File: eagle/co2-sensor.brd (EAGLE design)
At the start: 34 x 30 mm, 12 parts, among them IC1 LM1117IMPX-3.3, J1 MH-Z19, U1 esp12e, U2 dht22, X1 usb

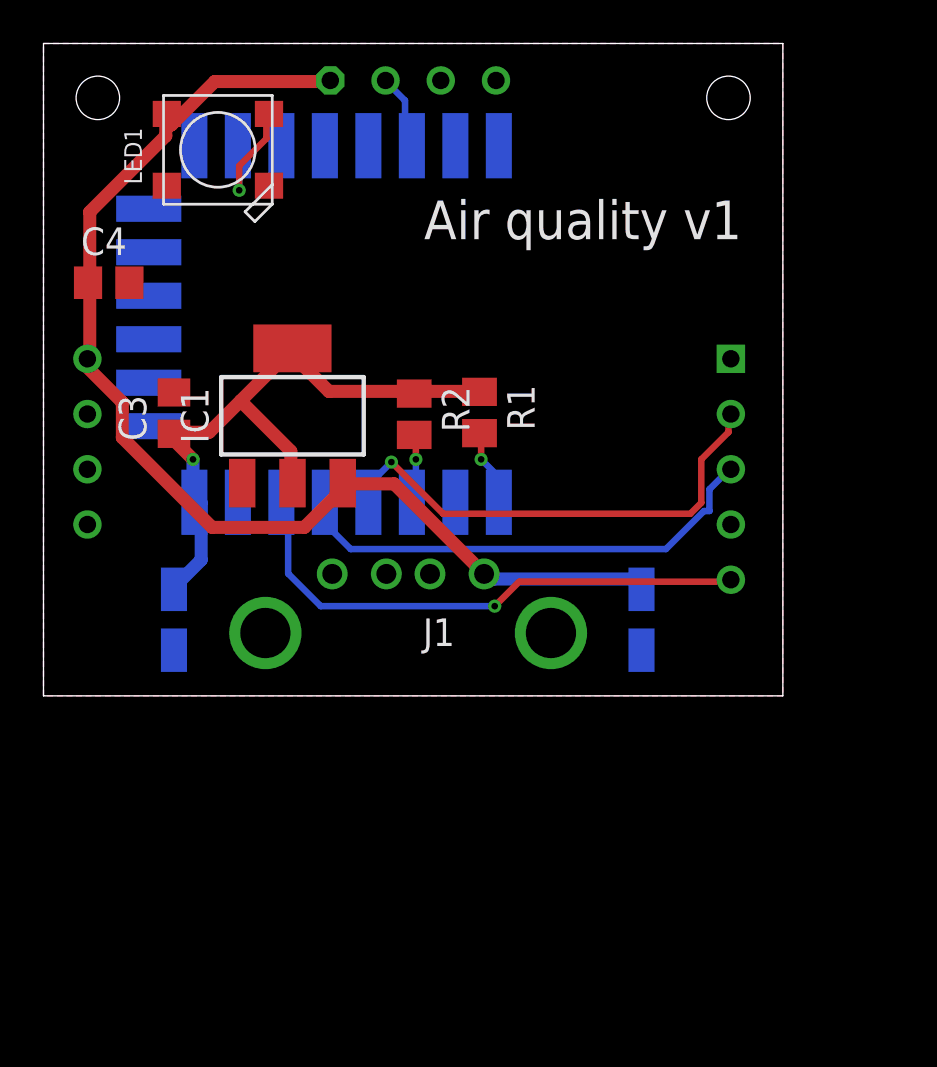
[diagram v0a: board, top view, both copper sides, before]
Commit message: fixed prototype issues
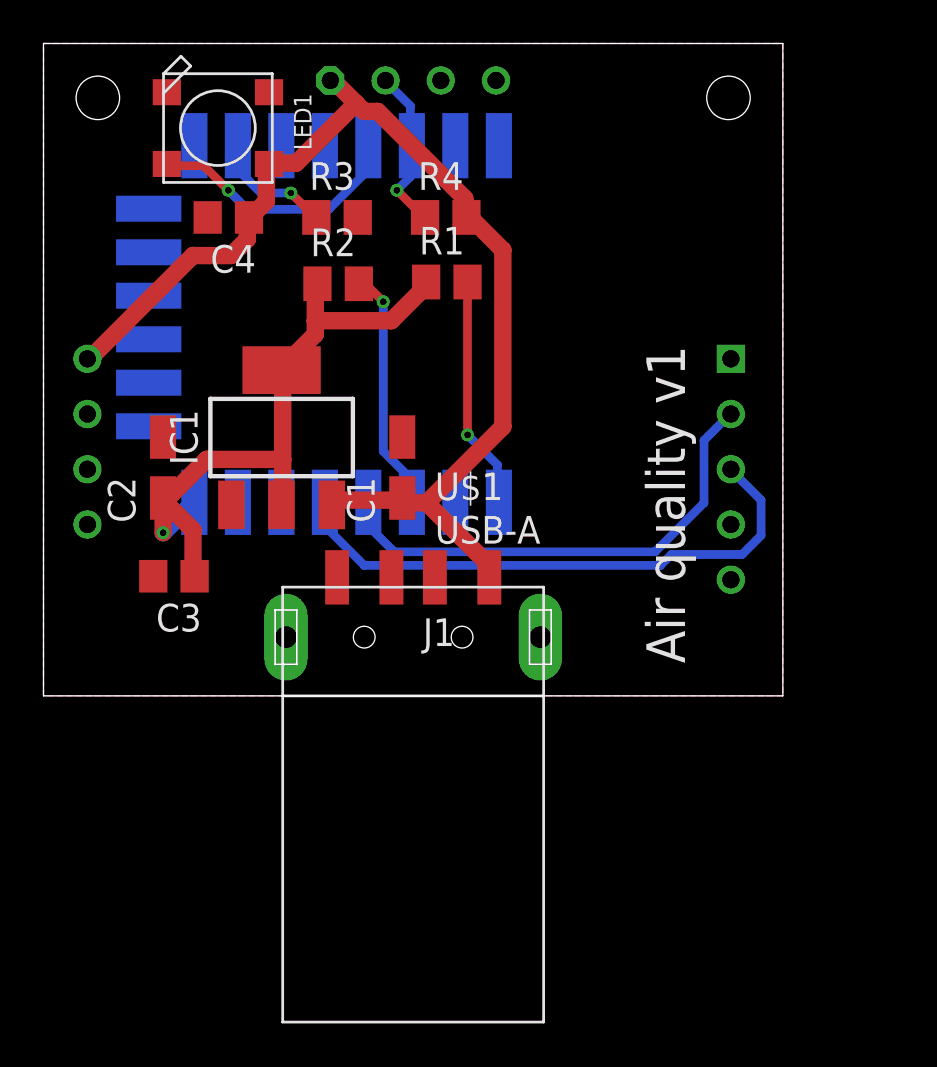
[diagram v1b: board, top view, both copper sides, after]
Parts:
- removed X1: usb, con-usb-3:USB-A-H
- added R3: 4.7k, rcl:M0805
- added R4: 10k, rcl:M0805
- added U$1: USB-A, usb:USB-A-SMT
- moved C1 13.0 mm to (16.5, 10.5), flipped to the top, turned to 90 degrees
- moved C3 7.50 mm to (6.00, 5.50), turned to 180 degrees
- moved C2 7.02 mm to (5.50, 10.5), flipped to the top, turned to 90 degrees
- moved R2 6.95 mm to (13.6, 18.9), turned to 0 degrees
- moved C4 6.26 mm to (8.50, 22.0), turned to 180 degrees
- moved R1 6.18 mm to (18.6, 19.0), turned to 0 degrees
- moved IC1 1.12 mm to (10.9, 11.9)
- moved LED1 1.00 mm to (8.02, 26.1), turned to 0 degrees
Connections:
- net CO2_VO renamed VO
- removed net CO2_HD: J1.5, U1.GPIO12
- removed net LED_DIN: LED1.4-DIN, U1.GPIO15
- new net LED: LED1.4-DIN, U1.GPIO4
- new net N$1: R3.1, U1.GPIO15
- net +5V: now also R4.2, U$1.P$6; no longer X1.VBUS
- net DHT22: now also R4.1
- net GND: now also R3.2, U$1.P$3; no longer X1.GND
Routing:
- net CO2_HD: track 25.0 -> 0.00 mm, vias 1 -> 0
- net LED: track 0.00 -> 12.0 mm, vias 0 -> 1
- net CH_PD: track 3.32 -> 11.3 mm
- net RESET: track 3.54 -> 10.7 mm
- net LED_DIN: track 6.22 -> 0.00 mm, vias 1 -> 0
- net N$1: track 0.00 -> 5.63 mm, vias 0 -> 1
- net DHT22: track 3.64 -> 7.64 mm, vias 0 -> 1
- net CO2_TX: track 22.2 -> 26.1 mm
- net +5V: track 54.7 -> 52.8 mm
- net +3V3: track 30.0 -> 31.0 mm
- net CO2_RX: track 22.4 -> 22.6 mm, vias 1 -> 0

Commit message: .
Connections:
- net GND: now also U$1.P$1, U$1.P$2
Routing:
- net CO2_TX: track 26.1 -> 22.7 mm, vias 0 -> 1
- net LED: track 12.0 -> 12.7 mm
- net +5V: track 52.8 -> 53.4 mm

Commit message: .
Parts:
- removed C1: 10mF, rcl:CT3216
- added BT1: BAT-HLD-012-SMT, BAT-HLD-012-SMT:BAT_BAT-HLD-012-SMT
- added IC2: (no value), DS3231_industrialberry:SOIC-16W
- added JP1: (no value), pinhead:1X04
- added JP2: (no value), pinhead:2X04
- added R5, R6: 4.7k, rcl:M0805
- C4: value 100n -> 10u
- LED1: value WS2812B_5050N -> WS2812B5050; device WS2812B:WS2812B-NARROW -> WS2812B:WS2812B
- U$1: value USB-A -> USB-C; device usb:USB-A-SMT -> USB-C:USB-C
- moved J1 50.0 mm to (19.5, 46.5), turned to 270 degrees
- moved U$1 45.0 mm to (26.5, 44.0), flipped to the bottom, turned to 180 degrees
- moved C2 33.7 mm to (31.0, 32.5), flipped to the bottom
- moved C3 33.3 mm to (31.0, 27.5), flipped to the bottom, turned to 270 degrees
- moved C4 22.6 mm to (27.0, 35.0), flipped to the bottom, turned to 0 degrees
- moved IC1 22.5 mm to (25.5, 29.0), flipped to the bottom, turned to 180 degrees
- moved R4 19.0 mm to (19.0, 41.0), flipped to the bottom, turned to 90 degrees
- moved U2 14.1 mm to (12.0, 41.5)
- moved LED1 10.9 mm to (17.5, 31.5), flipped to the bottom, turned to 180 degrees
- moved R1 4.53 mm to (14.5, 17.0), flipped to the bottom, turned to 270 degrees
- moved R3 3.64 mm to (17.0, 21.0), flipped to the bottom, turned to 270 degrees
- moved R2 2.49 mm to (12.0, 17.0), flipped to the bottom, turned to 270 degrees
- moved U1 1.91 mm to (14.5, 19.0), flipped to the top
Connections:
- removed net LED: LED1.4-DIN, U1.GPIO4
- removed net RESET: R1.2, U1.RESET
- new net CLOCK_INT: IC2.3, U1.GPIO13
- new net IO0: JP2.5, U1.GPIO0
- new net IO2: JP2.3, LED1.4-DIN, U1.GPIO2
- new net N$6: BT1.P1, BT1.P2, IC2.14
- new net RST: IC2.4, JP2.6, R2.2, U1.RESET
- new net RXD: JP2.7, U1.RXD0
- new net SCL: IC2.16, JP1.3, R6.2, U1.GPIO5
- new net SDA: IC2.15, JP1.4, R5.2, U1.GPIO4
- new net TXD: JP2.2, U1.TXD0
- net +3V3: now also IC2.2, JP1.2, JP2.8, R5.1, R6.1
- net +5V: now also U$1.A9, U$1.B9; no longer C1.+, U$1.P$6
- net CH_PD: now also JP2.4, R1.2; no longer R2.2
- net DHT22: now also U1.GPIO12; no longer U1.GPIO5
- net GND: now also BT1.N, IC2.10, IC2.11, IC2.12, IC2.13, IC2.5, IC2.6, IC2.7, IC2.8, IC2.9, JP1.1, JP2.1, U$1.A12, U$1.B12, U$1.P$10, U$1.P$7, U$1.P$8, U$1.P$9; no longer C1.-, U$1.P$1, U$1.P$2, U$1.P$3
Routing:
- net RST: track 0.00 -> 78.8 mm, vias 0 -> 1
- net TXD: track 0.00 -> 44.4 mm
- net +3V3: track 31.1 -> 68.7 mm, vias 1 -> 2
- net DHT22: track 7.64 -> 43.9 mm
- net SDA: track 0.00 -> 35.5 mm, vias 0 -> 2
- net SCL: track 0.00 -> 31.6 mm, vias 0 -> 2
- net N$6: track 0.00 -> 30.9 mm, vias 0 -> 1
- net RXD: track 0.00 -> 29.1 mm
- net CH_PD: track 11.3 -> 37.8 mm, vias 1 -> 2
- net IO2: track 0.00 -> 25.8 mm, vias 0 -> 1
- net IO0: track 0.00 -> 24.0 mm
- net +5V: track 53.4 -> 73.1 mm
- net CLOCK_INT: track 0.00 -> 12.7 mm, vias 0 -> 1
- net LED: track 12.7 -> 0.00 mm, vias 1 -> 0
- net RESET: track 10.7 -> 0.00 mm, vias 1 -> 0
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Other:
- board size 34 x 30 mm -> 40 x 44 mm
- board text removed: "Air quality v1"

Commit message: .
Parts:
- added C1: 100n, rcl:C0805
- added U3: BMP280, BMP280:XDCR_BMP280
- moved U2 39.6 mm to (31.5, 7.00)
- moved R4 39.3 mm to (29.0, 3.00), turned to 0 degrees
- moved R3 11.1 mm to (20.5, 31.5), turned to 90 degrees
- moved LED1 9.82 mm to (20.0, 22.0)
- moved IC2 8.06 mm to (33.5, 18.0)
- moved BT1 2.50 mm to (34.0, 18.0)
- moved R1 2.50 mm to (12.5, 15.5)
- moved R2 2.50 mm to (10.0, 15.5)
- moved R5 2.50 mm to (12.5, 22.5)
- moved R6 2.50 mm to (10.0, 22.5)
- moved C3 1.00 mm to (31.0, 26.5)
- moved JP2 1.00 mm to (36.5, 33.0)
- moved C2 0.50 mm to (31.0, 32.0)
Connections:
- net +3V3: now also C1.1, U3.2, U3.6, U3.8
- net GND: now also C1.2, U3.1, U3.5, U3.7
- net SCL: now also U3.4
- net SDA: now also U3.3
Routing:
- net +3V3: track 68.7 -> 105.4 mm, vias 2 -> 0
- net SDA: track 35.5 -> 71.0 mm
- net SCL: track 31.6 -> 62.3 mm, vias 2 -> 4
- net DHT22: track 43.9 -> 20.8 mm, vias 1 -> 0
- net RST: track 78.8 -> 67.2 mm, vias 1 -> 2
- net CLOCK_INT: track 12.7 -> 21.7 mm, vias 1 -> 3
- net CH_PD: track 37.8 -> 46.7 mm, vias 2 -> 1
- net N$6: track 30.9 -> 25.8 mm
- net +5V: track 73.1 -> 69.8 mm, vias 0 -> 3
- net N$1: track 6.72 -> 3.55 mm
- net IO2: track 25.8 -> 23.3 mm
- net CO2_TX: track 28.7 -> 30.9 mm, vias 1 -> 0
- net CO2_RX: track 29.5 -> 31.7 mm, vias 0 -> 1
- net IO0: track 24.0 -> 22.5 mm
- net TXD: track 44.4 -> 45.4 mm
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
